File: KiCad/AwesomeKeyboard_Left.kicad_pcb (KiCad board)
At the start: 2 copper layers, 140 x 109 mm, 56 parts, among them J1 AudioJack4_Ground, SW1 SW_DIP_x01, SW11 SW_Push, SW12 SW_Push, SW13 SW_Push, SW14 SW_Push, SW15 SW_Push, SW16 SW_Push, SW21 SW_Push, SW22 SW_Push, SW23 SW_Push, SW24 SW_Push, SW25 SW_Push, SW26 SW_Push, SW31 SW_Push, SW32 SW_Push, SW33 SW_Push, SW34 SW_Push, SW35 SW_Push, SW36 SW_Push, SW45 SW_Push, SW46 SW_Push

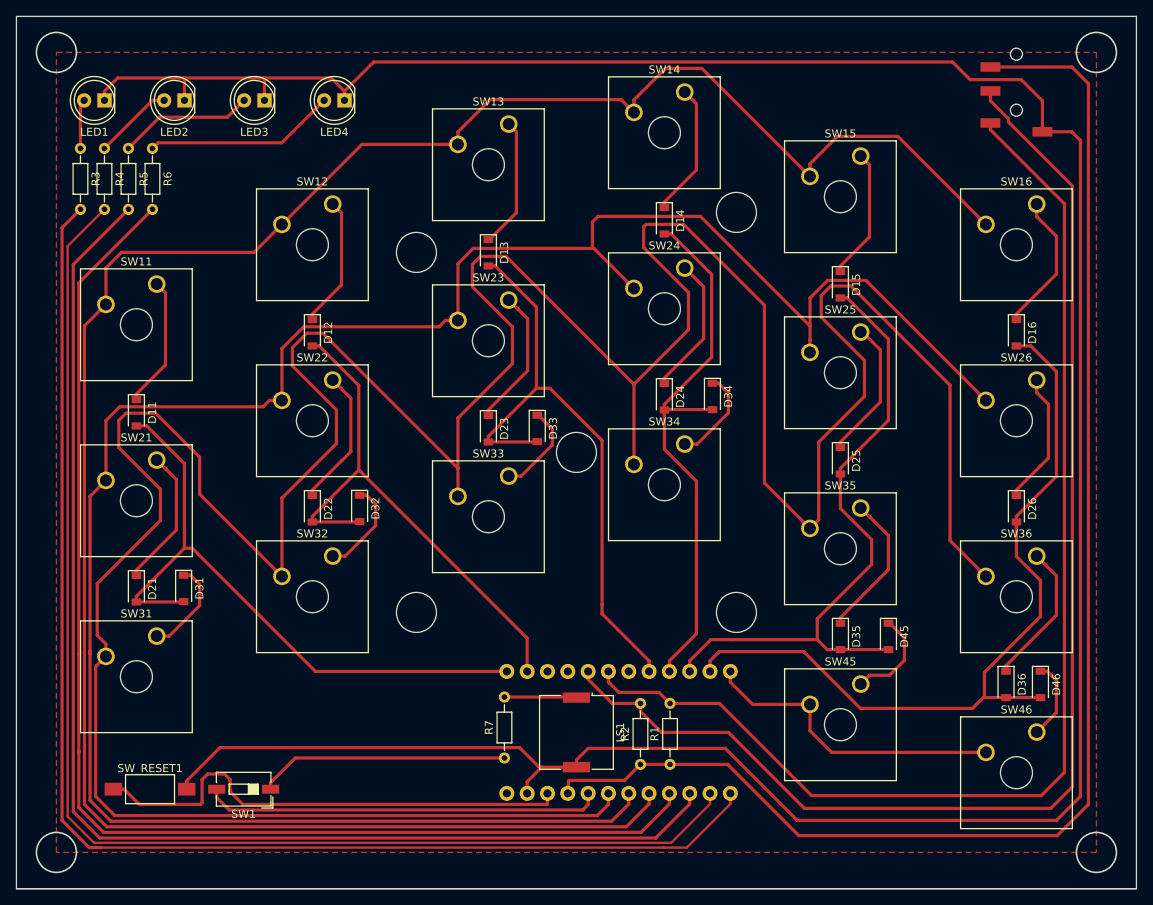
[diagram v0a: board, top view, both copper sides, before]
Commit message: add bypass condenser
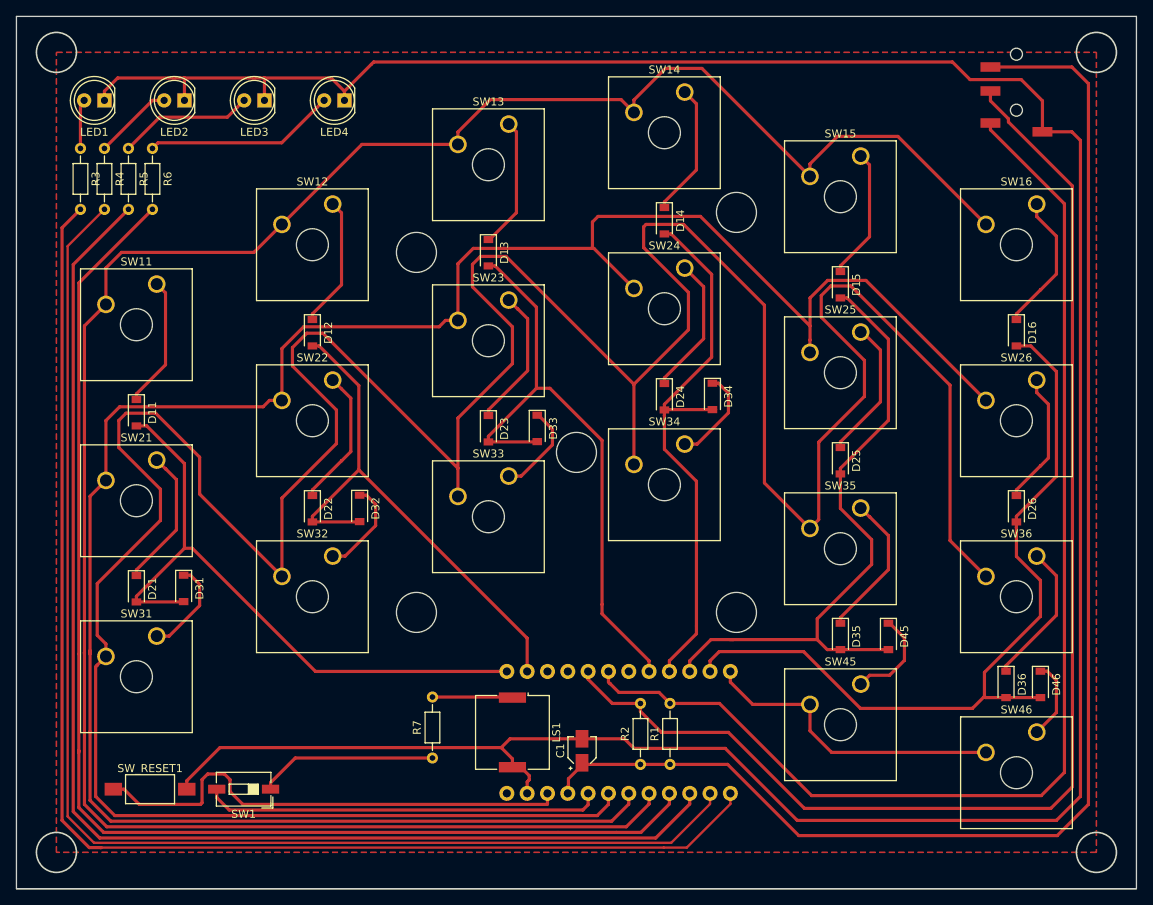
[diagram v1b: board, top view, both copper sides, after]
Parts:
- added C1: C, Capacitor_SMD:CP_Elec_3x5.3, F.Cu at (143.5, 162.0)
- moved R7 9.00 mm to (124.8, 162.9)
- moved LS1 8.00 mm to (134.8, 159.7)
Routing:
- net Net-(R7-Pad1): track 31.3 -> 22.3 mm
- net GND: track 347.1 -> 349.4 mm
- net Net-(LS1-Pad1): track 9.03 -> 10.0 mm
- net VCC: track 175.9 -> 176.5 mm
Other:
- net class Default: trace_width 0.3 -> 0.4
